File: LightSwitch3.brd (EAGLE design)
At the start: 22 x 62 mm, 7 parts, among them SW1 SWITCH-SPST-ILLUMINATED, SW2 SWITCH-SPST-ILLUMINATED, SW3 SWITCH-SPST-ILLUMINATED

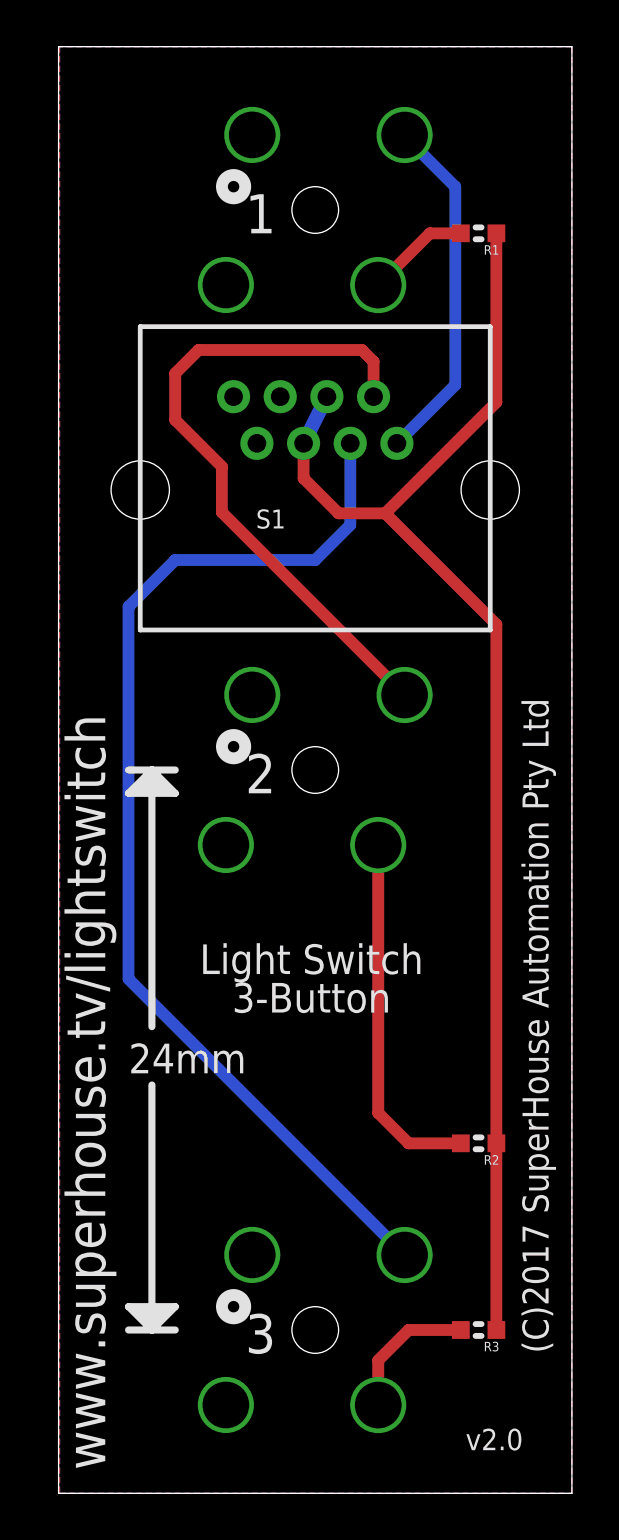
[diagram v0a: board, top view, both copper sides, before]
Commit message: Changed button footprint to slotted version for v2.1 release
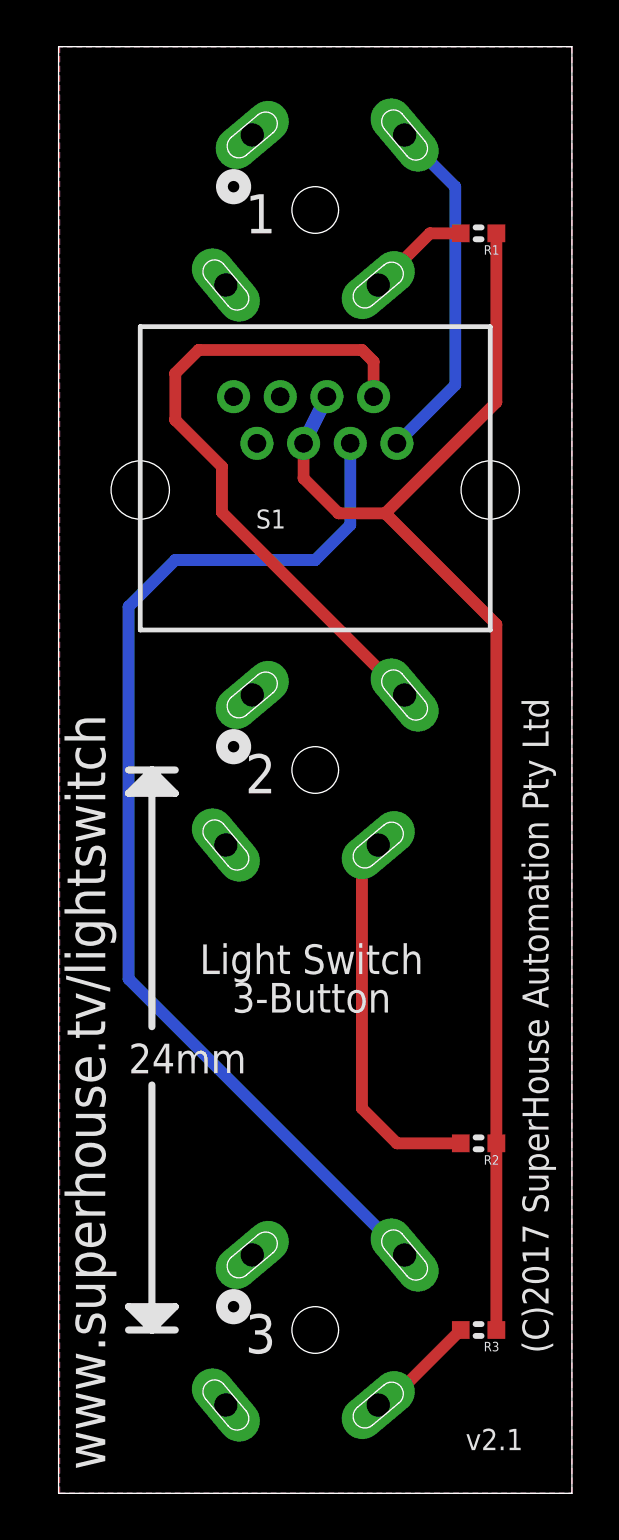
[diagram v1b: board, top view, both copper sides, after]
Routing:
- net N$6: track 5.99 -> 4.87 mm
- net N$3: track 15.6 -> 16.4 mm
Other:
- board text added: "v2.1"
- board text removed: "v2.0"
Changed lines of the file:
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@@
 <?xml version="1.0" encoding="utf-8"?>
 <!DOCTYPE eagle SYSTEM "eagle.dtd">
-<eagle version="8.3.2">
+<eagle version="8.7.0">
 <drawing>
 <settings>
-<setting alwaysvectorfont="yes"/>
+<setting alwaysvectorfont="no"/>
 <setting keepoldvectorfont="yes"/>
 <setting verticaltext="up"/>
@@
 <layer number="60" name="p_dimension" color="6" fill="0" visible="no" active="no"/>
 <layer number="61" name="pt_docu" color="7" fill="0" visible="no" active="no"/>
+<layer number="88" name="SimResults" color="9" fill="1" visible="no" active="no"/>
+<layer number="89" name="SimProbes" color="9" fill="1" visible="no" active="no"/>
 <layer number="90" name="Modules" color="7" fill="1" visible="no" active="no"/>
 <layer number="91" name="Nets" color="2" fill="1" visible="no" active="no"/>
@@
 <wire x1="22" y1="62" x2="22" y2="0" width="0" layer="20"/>
 <text x="21" y="6" size="1.1176" layer="21" font="vector" ratio="15" rot="R90">(C)2017 SuperHouse Automation Pty Ltd</text>
-<text x="17.4452" y="1.8486" size="0.9144" layer="21" font="vector" ratio="15">v2.0</text>
+<text x="17.4452" y="1.8486" size="0.9144" layer="21" font="vector" ratio="15">v2.1</text>
 <text x="10.8412" y="22.0646" size="1.27" layer="21" font="vector" ratio="15" distance="30" align="center">Light Switch
 3-Button</text>
-<text x="2" y="1" size="1.6764" layer="21" ratio="15" rot="R90">www.superhouse.tv/lightswitch</text>
-<text x="8" y="54" size="1.6764" layer="21" ratio="15">1</text>
-<text x="8" y="30" size="1.6764" layer="21" ratio="15">2</text>
-<text x="8" y="6" size="1.6764" layer="21" ratio="15">3</text>
-<text x="3" y="18" size="1.27" layer="21" ratio="15">24mm</text>
+<text x="2" y="1" size="1.6764" layer="21" font="vector" ratio="15" rot="R90">www.superhouse.tv/lightswitch</text>
+<text x="8" y="54" size="1.6764" layer="21" font="vector" ratio="15">1</text>
+<text x="8" y="30" size="1.6764" layer="21" font="vector" ratio="15">2</text>
+<text x="8" y="6" size="1.6764" layer="21" font="vector" ratio="15">3</text>
+<text x="3" y="18" size="1.27" layer="21" font="vector" ratio="15">24mm</text>
 <wire x1="3" y1="31" x2="4" y2="31" width="0.3048" layer="21"/>
 <wire x1="4" y1="31" x2="5" y2="31" width="0.3048" layer="21"/>
@@
 <param name="dpMaxLengthDifference" value="10mm"/>
 <param name="dpGapFactor" value="2.5"/>
-<param name="checkGrid" value="0"/>
 <param name="checkAngle" value="0"/>
 <param name="checkFont" value="1"/>
 <param name="checkRestrict" value="1"/>
+<param name="checkStop" value="0"/>
+<param name="checkValues" value="0"/>
 <param name="useDiameter" value="13"/>
 <param name="maxErrors" value="50"/>
@@
 <contactref element="SW2" pad="2"/>
 <contactref element="R2" pad="2"/>
-<wire x1="17.238" y1="15" x2="15" y2="15" width="0.508" layer="1"/>
-<wire x1="15" y1="15" x2="13.699709375" y2="16.300290625" width="0.508" layer="1"/>
-<wire x1="13.699709375" y1="16.300290625" x2="13.699709375" y2="27.7826125" width="0.508" layer="1"/>
+<wire x1="17.238" y1="15" x2="14.5" y2="15" width="0.508" layer="1"/>
+<wire x1="14.5" y1="15" x2="13" y2="16.5" width="0.508" layer="1"/>
+<wire x1="13" y1="27.082903125" x2="13.699709375" y2="27.7826125" width="0.508" layer="1"/>
+<wire x1="13" y1="16.5" x2="13" y2="27.082903125" width="0.508" layer="1"/>
 </signal>
 <signal name="N$6">
 <contactref element="SW3" pad="2"/>
 <contactref element="R3" pad="2"/>
-<wire x1="17.238" y1="7" x2="15" y2="7" width="0.508" layer="1"/>
-<wire x1="15" y1="7" x2="13.699709375" y2="5.699709375" width="0.508" layer="1"/>
-<wire x1="13.699709375" y1="5.699709375" x2="13.699709375" y2="3.7826125" width="0.508" layer="1"/>
+<wire x1="17.238" y1="7" x2="14.0206125" y2="3.7826125" width="0.508" layer="1"/>
+<wire x1="14.0206125" y1="3.7826125" x2="13.699709375" y2="3.7826125" width="0.508" layer="1"/>
 </signal>
 </signals>
-<errors>
-</errors>
 </board>
 </drawing>

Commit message: Updated RJ45 footprint for v2.2
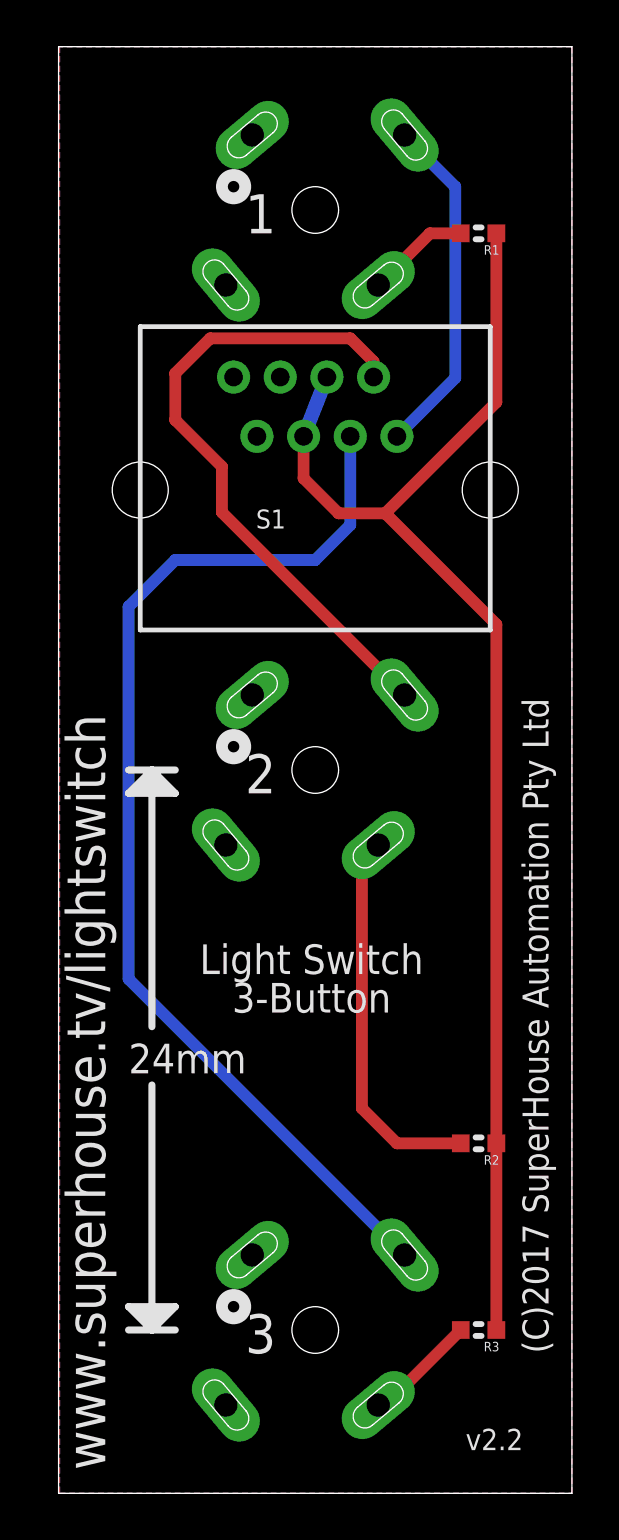
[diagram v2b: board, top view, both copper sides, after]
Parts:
- R1, R2, R3: value 3K3 -> 4K7
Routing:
- net +12V: track 58.8 -> 59.6 mm
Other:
- board text added: "v2.2"
- board text removed: "v2.1"
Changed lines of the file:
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@@
 <wire x1="22" y1="62" x2="22" y2="0" width="0" layer="20"/>
 <text x="21" y="6" size="1.1176" layer="21" font="vector" ratio="15" rot="R90">(C)2017 SuperHouse Automation Pty Ltd</text>
-<text x="17.4452" y="1.8486" size="0.9144" layer="21" font="vector" ratio="15">v2.1</text>
+<text x="17.4452" y="1.8486" size="0.9144" layer="21" font="vector" ratio="15">v2.2</text>
 <text x="10.8412" y="22.0646" size="1.27" layer="21" font="vector" ratio="15" distance="30" align="center">Light Switch
 3-Button</text>
@@
 <elements>
 <element name="S1" library="freetronics-jon" package="RJ45" value="RJ45" x="11" y="43"/>
-<element name="R1" library="freetronics-jon" package="0603" value="3K3" x="18" y="54" rot="R180"/>
-<element name="R2" library="freetronics-jon" package="0603" value="3K3" x="18" y="15" rot="R180"/>
-<element name="R3" library="freetronics-jon" package="0603" value="3K3" x="18" y="7" rot="R180"/>
+<element name="R1" library="freetronics-jon" package="0603" value="4K7" x="18" y="54" rot="R180"/>
+<element name="R2" library="freetronics-jon" package="0603" value="4K7" x="18" y="15" rot="R180"/>
+<element name="R3" library="freetronics-jon" package="0603" value="4K7" x="18" y="7" rot="R180"/>
 <element name="SW1" library="freetronics-jon" package="SWITCH-SPST-ILLUMINATED" value="SWITCH-SPST-ILLUMINATED" x="11" y="55" rot="MR50"/>
 <element name="SW2" library="freetronics-jon" package="SWITCH-SPST-ILLUMINATED" value="SWITCH-SPST-ILLUMINATED" x="11" y="31" rot="MR50"/>
@@
 <contactref element="S1" pad="5"/>
 <contactref element="S1" pad="4"/>
-<wire x1="10.5" y1="45" x2="11.5" y2="47" width="0.6096" layer="16"/>
+<wire x1="10.5" y1="45.3" x2="11.5" y2="47.84" width="0.6096" layer="16"/>
 <contactref element="R1" pad="1"/>
 <contactref element="R2" pad="1"/>
 <contactref element="R3" pad="1"/>
-<wire x1="10.5" y1="45" x2="10.5" y2="43.5" width="0.508" layer="1"/>
+<wire x1="10.5" y1="45.3" x2="10.5" y2="43.5" width="0.508" layer="1"/>
 <wire x1="18.762" y1="15" x2="18.762" y2="7" width="0.508" layer="1"/>
 <wire x1="18.762" y1="54" x2="18.762" y2="46.762" width="0.508" layer="1"/>
@@
 <contactref element="S1" pad="1"/>
 <contactref element="SW1" pad="3"/>
-<wire x1="14.5" y1="45" x2="17" y2="47.5" width="0.508" layer="16"/>
-<wire x1="17" y1="47.5" x2="17" y2="56" width="0.508" layer="16"/>
-<wire x1="17" y1="56" x2="14.830225" y2="58.169775" width="0.508" layer="16"/>
+<wire x1="14.830225" y1="58.169775" x2="17" y2="56" width="0.508" layer="16"/>
 <wire x1="14.830225" y1="58.169775" x2="14.830225" y2="58.2139375" width="0.508" layer="16"/>
+<wire x1="17" y1="47.8" x2="14.5" y2="45.3" width="0.508" layer="16"/>
+<wire x1="17" y1="56" x2="17" y2="47.8" width="0.508" layer="16"/>
 </signal>
 <signal name="N$5">
 <contactref element="S1" pad="2"/>
-<wire x1="13.5" y1="47" x2="13.5" y2="48.5" width="0.508" layer="1"/>
-<wire x1="13.5" y1="48.5" x2="13" y2="49" width="0.508" layer="1"/>
-<wire x1="13" y1="49" x2="6" y2="49" width="0.508" layer="1"/>
-<wire x1="6" y1="49" x2="5" y2="48" width="0.508" layer="1"/>
 <wire x1="5" y1="48" x2="5" y2="46" width="0.508" layer="1"/>
 <wire x1="7" y1="44" x2="5" y2="46" width="0.508" layer="1"/>
@@
 <wire x1="7" y1="42.0441625" x2="7" y2="44" width="0.508" layer="1"/>
 <wire x1="14.830225" y1="34.2139375" x2="7" y2="42.0441625" width="0.508" layer="1"/>
+<wire x1="13.5" y1="47.84" x2="13.5" y2="48.5" width="0.508" layer="1"/>
+<wire x1="13.5" y1="48.5" x2="12.5" y2="49.5" width="0.508" layer="1"/>
+<wire x1="6.5" y1="49.5" x2="5" y2="48" width="0.508" layer="1"/>
+<wire x1="12.5" y1="49.5" x2="6.5" y2="49.5" width="0.508" layer="1"/>
 </signal>
 <signal name="N$2">
@@
 <wire x1="5" y1="40" x2="11" y2="40" width="0.508" layer="16"/>
 <wire x1="11" y1="40" x2="12.5" y2="41.5" width="0.508" layer="16"/>
-<wire x1="12.5" y1="41.5" x2="12.5" y2="45" width="0.508" layer="16"/>
+<wire x1="12.5" y1="41.5" x2="12.5" y2="45.3" width="0.508" layer="16"/>
 <contactref element="SW3" pad="3"/>
 <wire x1="3" y1="22.0441625" x2="14.830225" y2="10.2139375" width="0.508" layer="16"/>
